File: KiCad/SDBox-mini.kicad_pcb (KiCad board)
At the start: 2 copper layers, 36.1 x 34 mm, 27 parts, among them J1 DB25_Male, J2 Conn_02x03_Odd_Even, J3 Micro_SD_Card, J4 USB_B_Micro, U1 LM1117-3.3, U2 ATmega328P-AU, U3 74LVC3G17, U4 74HCT2G17, Y1 Crystal_GND24_Small

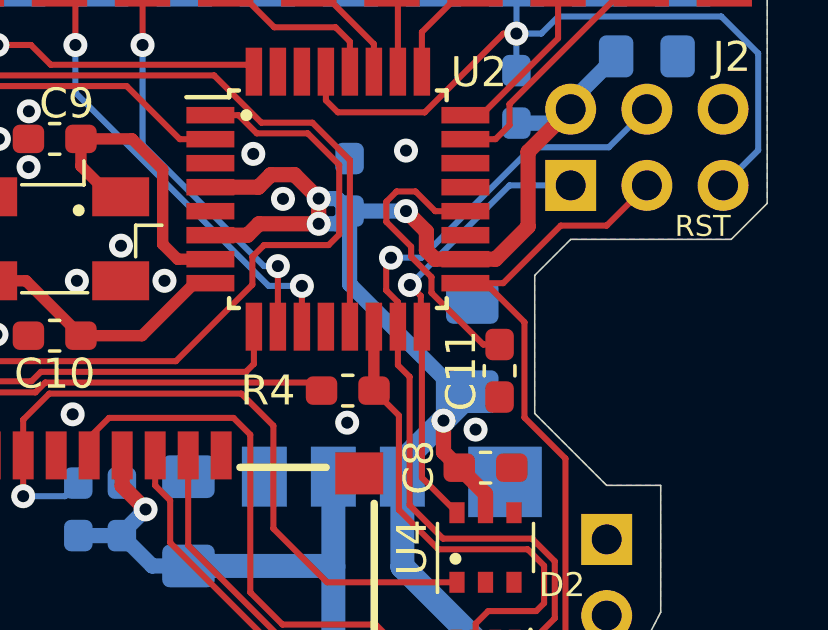
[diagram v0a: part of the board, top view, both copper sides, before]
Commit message: removed AREF capacitor, it was unnecessary
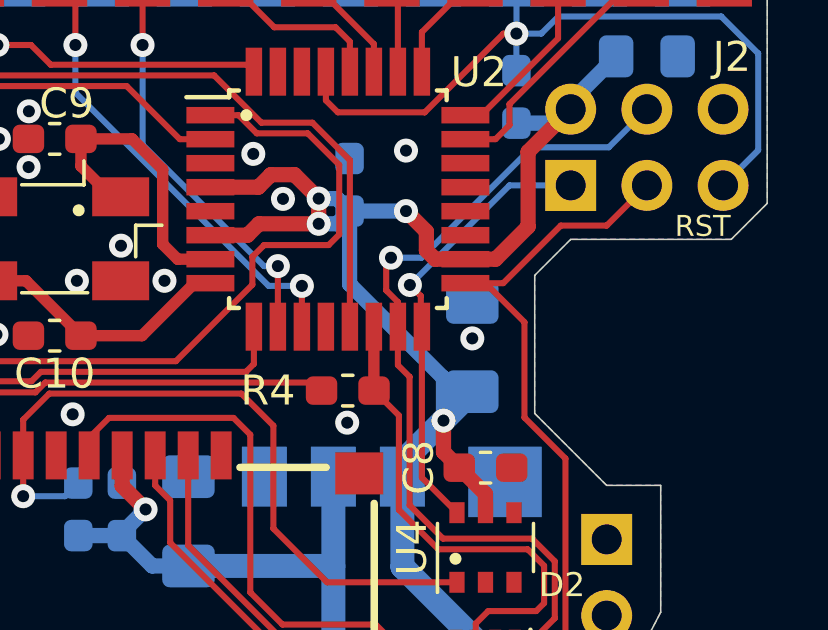
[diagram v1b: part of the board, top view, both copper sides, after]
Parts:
- removed C11: 0.1uF, Capacitor_SMD:C_0603_1608Metric_Pad1.05x0.95mm_HandSolder
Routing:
- net /AREF: track 9.69 -> 0.00 mm

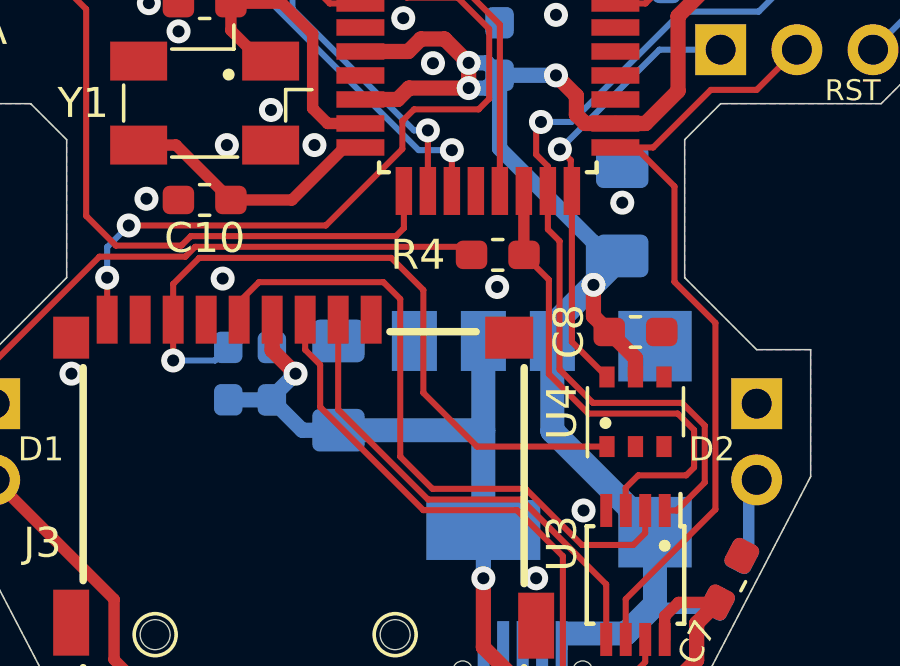
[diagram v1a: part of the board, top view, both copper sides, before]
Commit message: changed Activity-LED to be controlled by PB0, added 10k pull-up resistor on SS-line
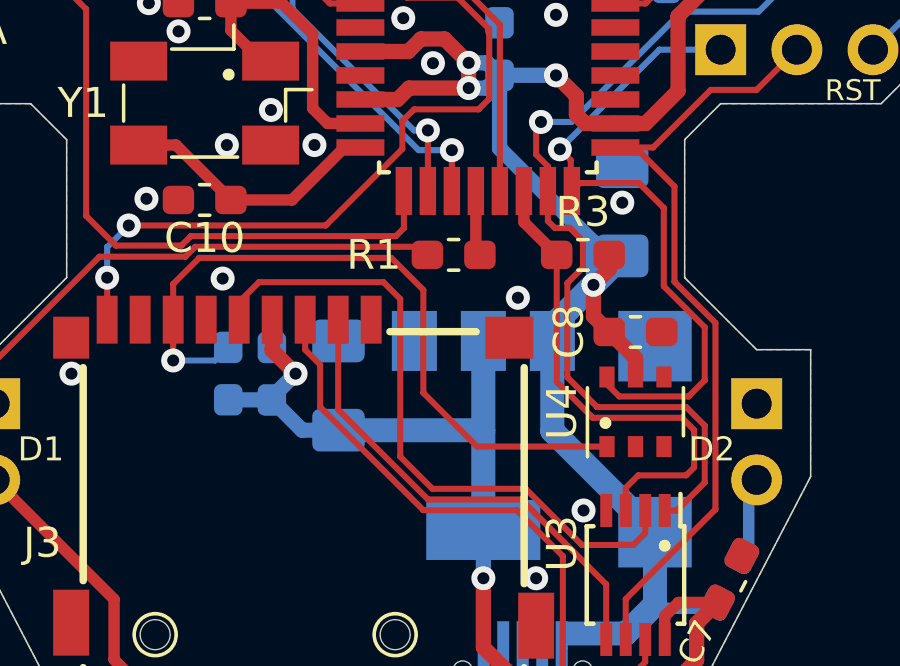
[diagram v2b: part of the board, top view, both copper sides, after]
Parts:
- added R3: 10k, Resistor_SMD:R_0603_1608Metric_Pad1.05x0.95mm_HandSolder, F.Cu at (113.4, 66.5)
- moved R1 1.47 mm to (109.1, 66.5)
- renumbered R4 to R1, R3 to R2, R2 to R4, R1 to R5
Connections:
- net /AREF renamed Net-(U2-Pad20)
- R1 pad 1: SS -> ACT_LED
- U2 pad 12: Net-(U2-Pad12) -> ACT_LED
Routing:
- net MISO: track 15.0 -> 22.0 mm
- net ACT_LED: track 0.00 -> 2.19 mm
- net Net-(D1-Pad1): track 19.4 -> 17.5 mm
- net VCC: track 87.6 -> 88.9 mm
- net MOSI: track 28.5 -> 29.2 mm

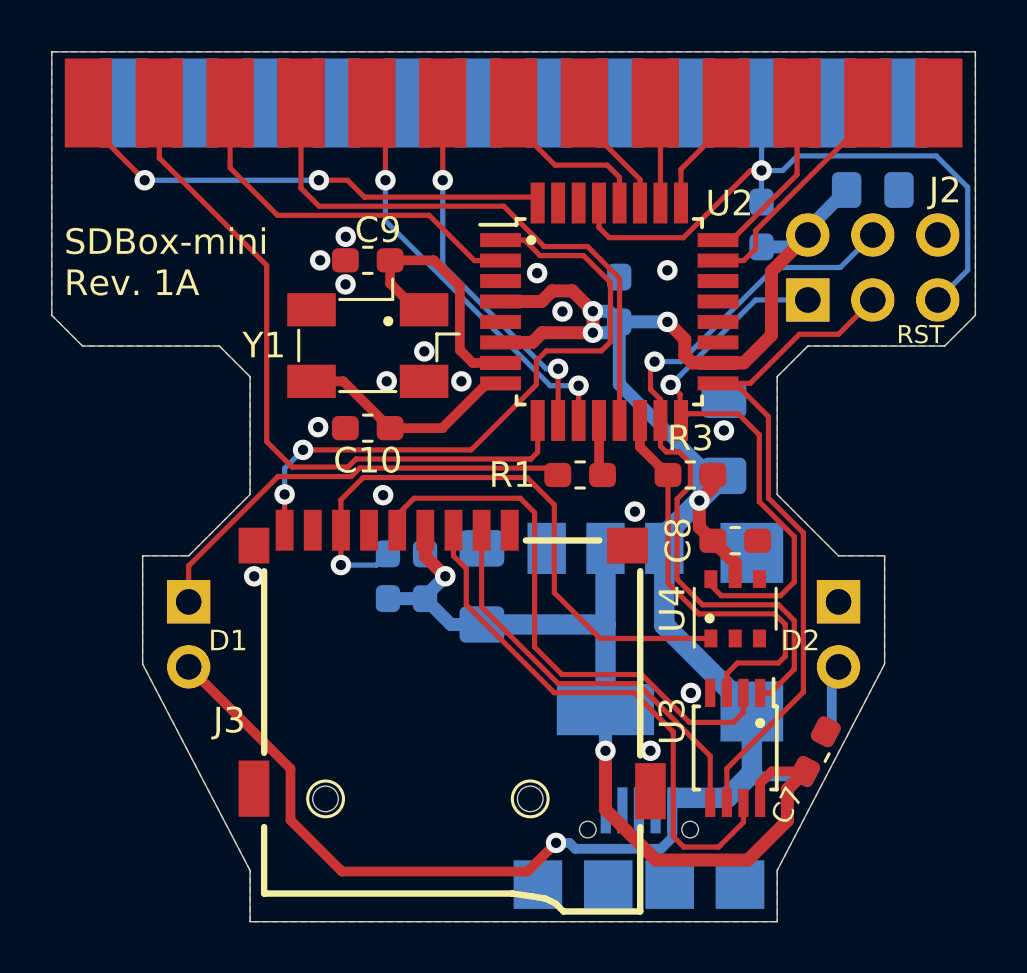
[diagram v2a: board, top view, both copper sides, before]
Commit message: Removed capacitor at VCC-pin ICSP-header and renumbered Caps
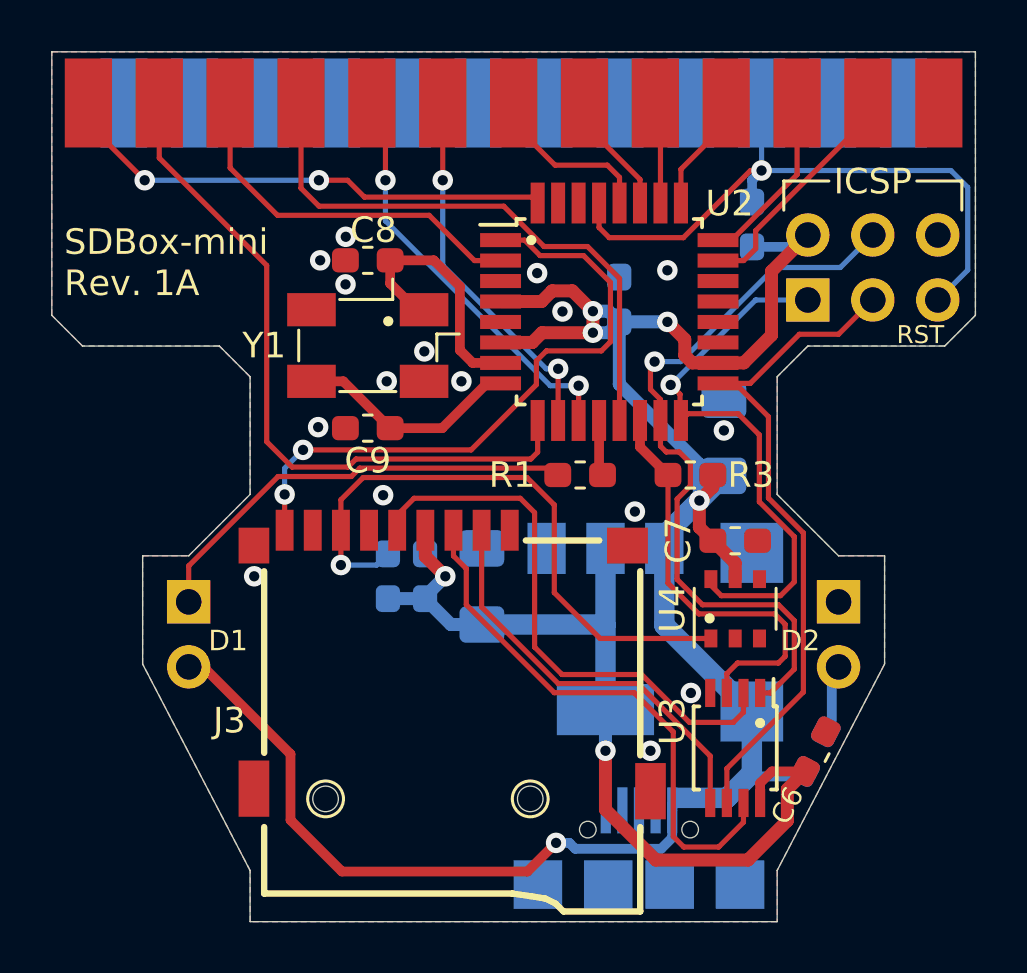
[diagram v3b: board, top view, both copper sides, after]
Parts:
- removed the C5 at (120.5, 55.4)
- moved R5 0.37 mm to (115.8, 56.8)
- renumbered C6 to C5, C7 to C6, C8 to C7, C9 to C8, C10 to C9
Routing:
- net VCC: track 88.9 -> 87.2 mm
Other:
- board text added: "ICSP"

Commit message: Changed U4 to a 74LVC1G17 and made SOT-353_SC-70-5_Custom_Handsoldering footprint
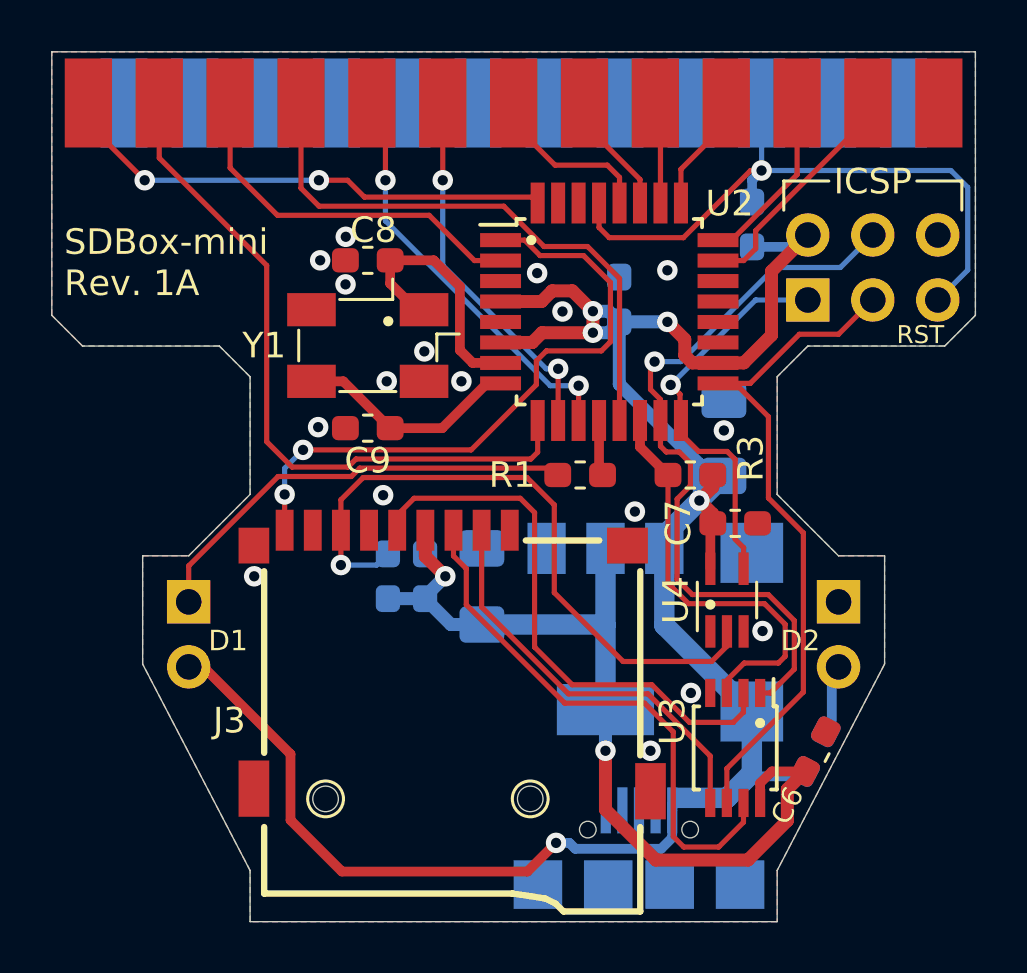
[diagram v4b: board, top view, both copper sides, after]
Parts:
- C1: value T491D227K010AT -> 220uF (T491D227K010AT)
- U4: value 74HCT2G17 -> 74LVC1G17; footprint Package_SO:TSOP-6_1.65x3.05mm_P0.95mm -> SDBox-mini:SOT-353_SC-70-5_Custom_Handsoldering
- moved C7 0.68 mm to (115.2, 68.4)
- moved U4 0.47 mm to (114.8, 71.4)
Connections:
- U4 pad 1: MISO_3V3 -> Net-(U4-Pad1)
- U4 pad 2: GND -> MISO_3V3
- U4 pad 4: Net-(U4-Pad4) -> MISO
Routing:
- net MISO: track 22.0 -> 15.8 mm
- net MISO_3V3: track 24.0 -> 25.8 mm
- net VCC: track 87.2 -> 86.4 mm
- net GND: vias 16 -> 17

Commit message: adapted TSSOP-8_3x3mm_P0.65mm footprint for Handsoldering
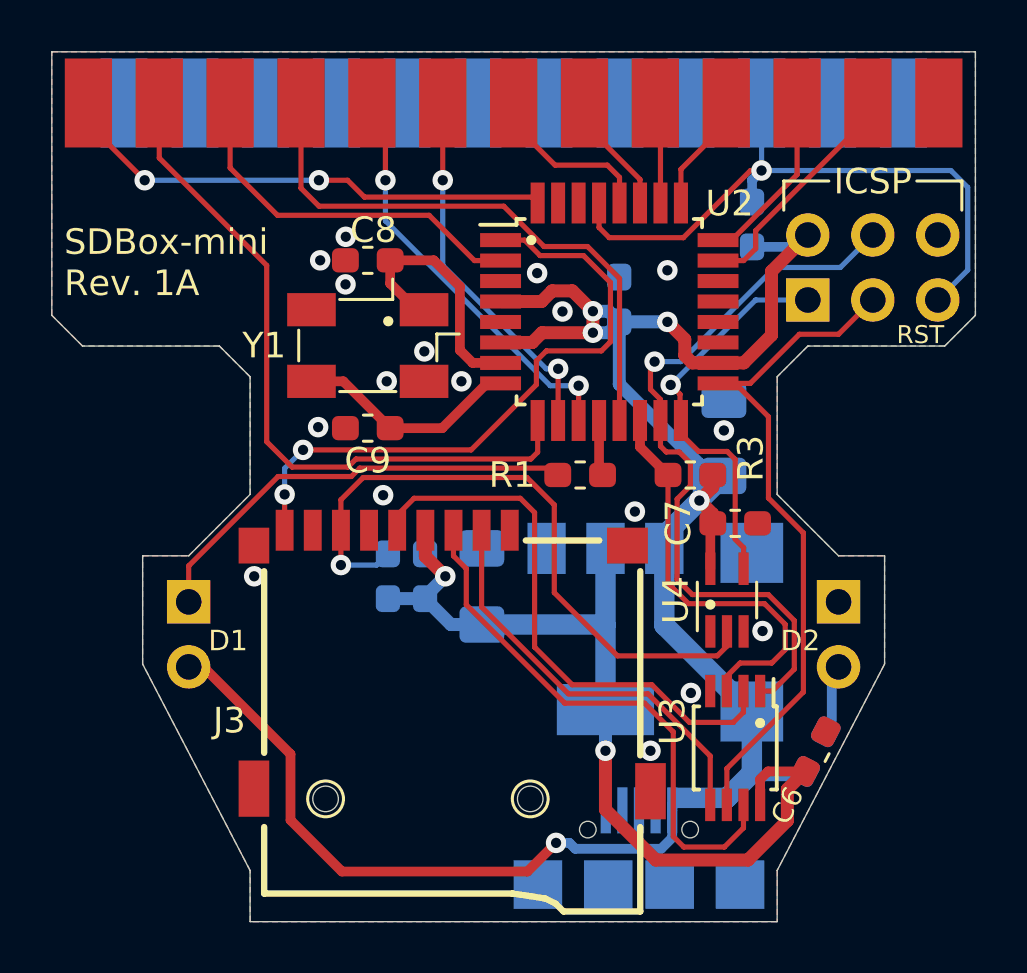
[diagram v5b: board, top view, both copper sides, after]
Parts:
- U3: footprint Package_SO:TSSOP-8_3x3mm_P0.65mm -> SDBox-mini:TSSOP-8_3x3mm_P0.65mm_Custom_Handsoldering

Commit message: added optional pull-up on MOSI, fixed keep-out area of copper pour on U3,U4 GND-pads to neighbouring pad
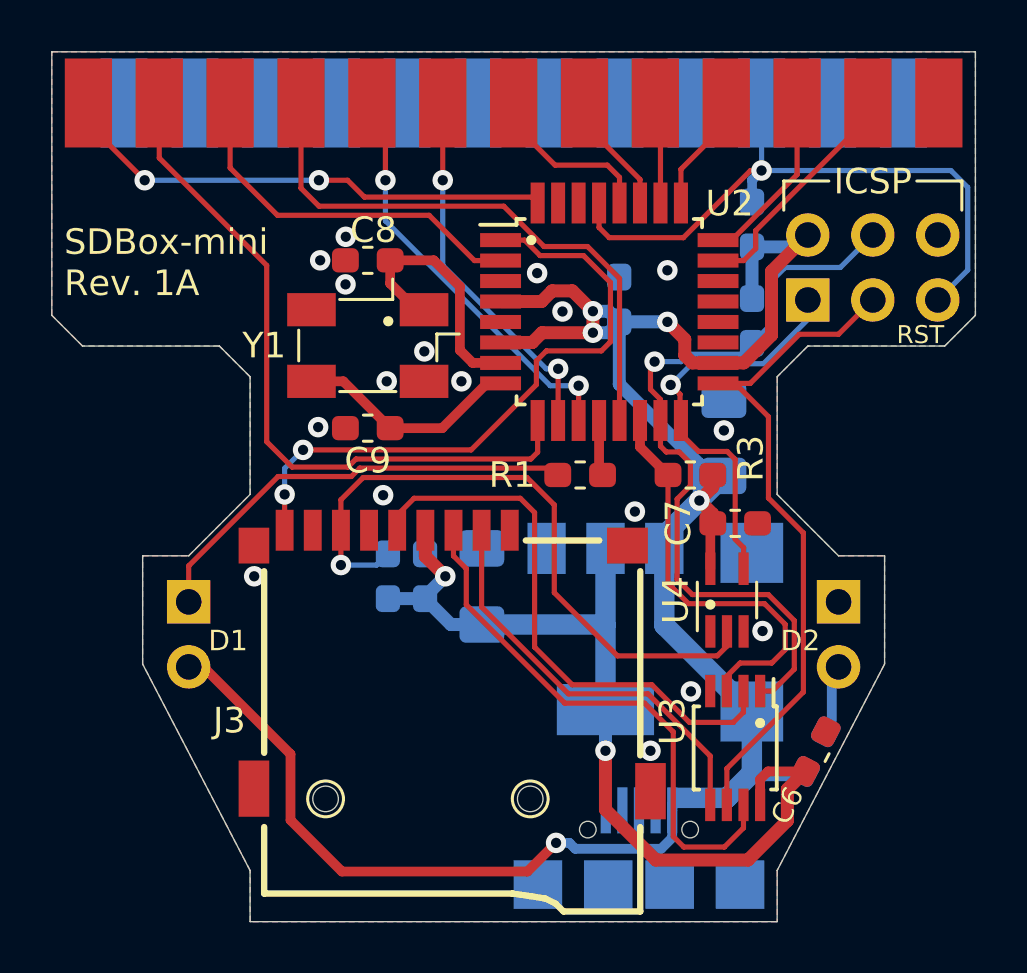
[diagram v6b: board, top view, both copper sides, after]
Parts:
- added R6: 10k, Resistor_SMD:R_0603_1608Metric_Pad1.05x0.95mm_HandSolder, B.Cu at (115.8, 60.5)
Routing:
- net VCC: track 86.4 -> 88.5 mm
- net MOSI: track 29.1 -> 30.1 mm

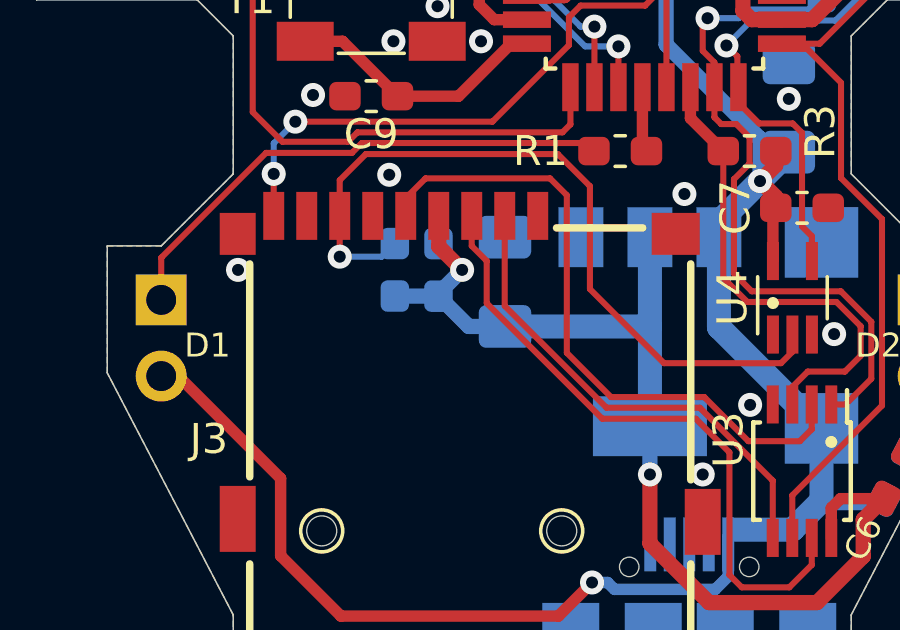
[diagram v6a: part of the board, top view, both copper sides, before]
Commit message: added common pull-up for DAT1,DAT2-lines (pin 8 and 1) on MicroSD-connector-pads
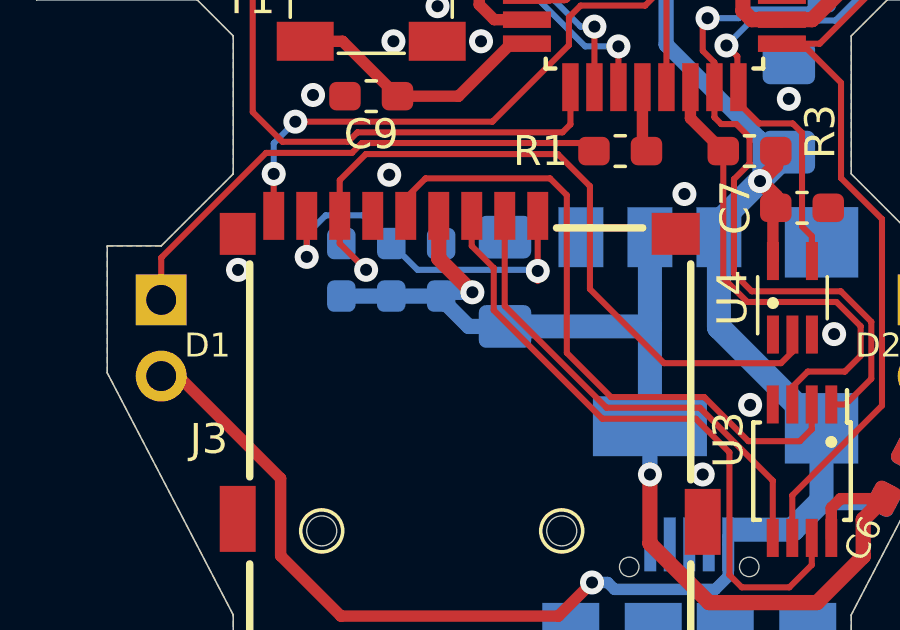
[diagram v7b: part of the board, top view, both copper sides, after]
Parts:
- added R5: 10k, Resistor_SMD:R_0603_1608Metric_Pad1.05x0.95mm_HandSolder, B.Cu at (101.5, 70.5)
- moved R4 1.78 mm to (99.8, 70.5)
- moved C4 0.09 mm to (103.1, 70.5)
- renumbered R5 to R7
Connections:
- J3 pad 8: Net-(J3-Pad8) -> Net-(J3-Pad1)
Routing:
- net Net-(J3-Pad1): track 0.00 -> 13.0 mm, vias 0 -> 2
- net 3V3: track 36.1 -> 38.3 mm
